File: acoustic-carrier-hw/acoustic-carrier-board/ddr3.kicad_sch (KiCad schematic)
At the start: 28 parts, among them IC1 ECP5-BGA256, IC2 MT41K256M16TW-107_P

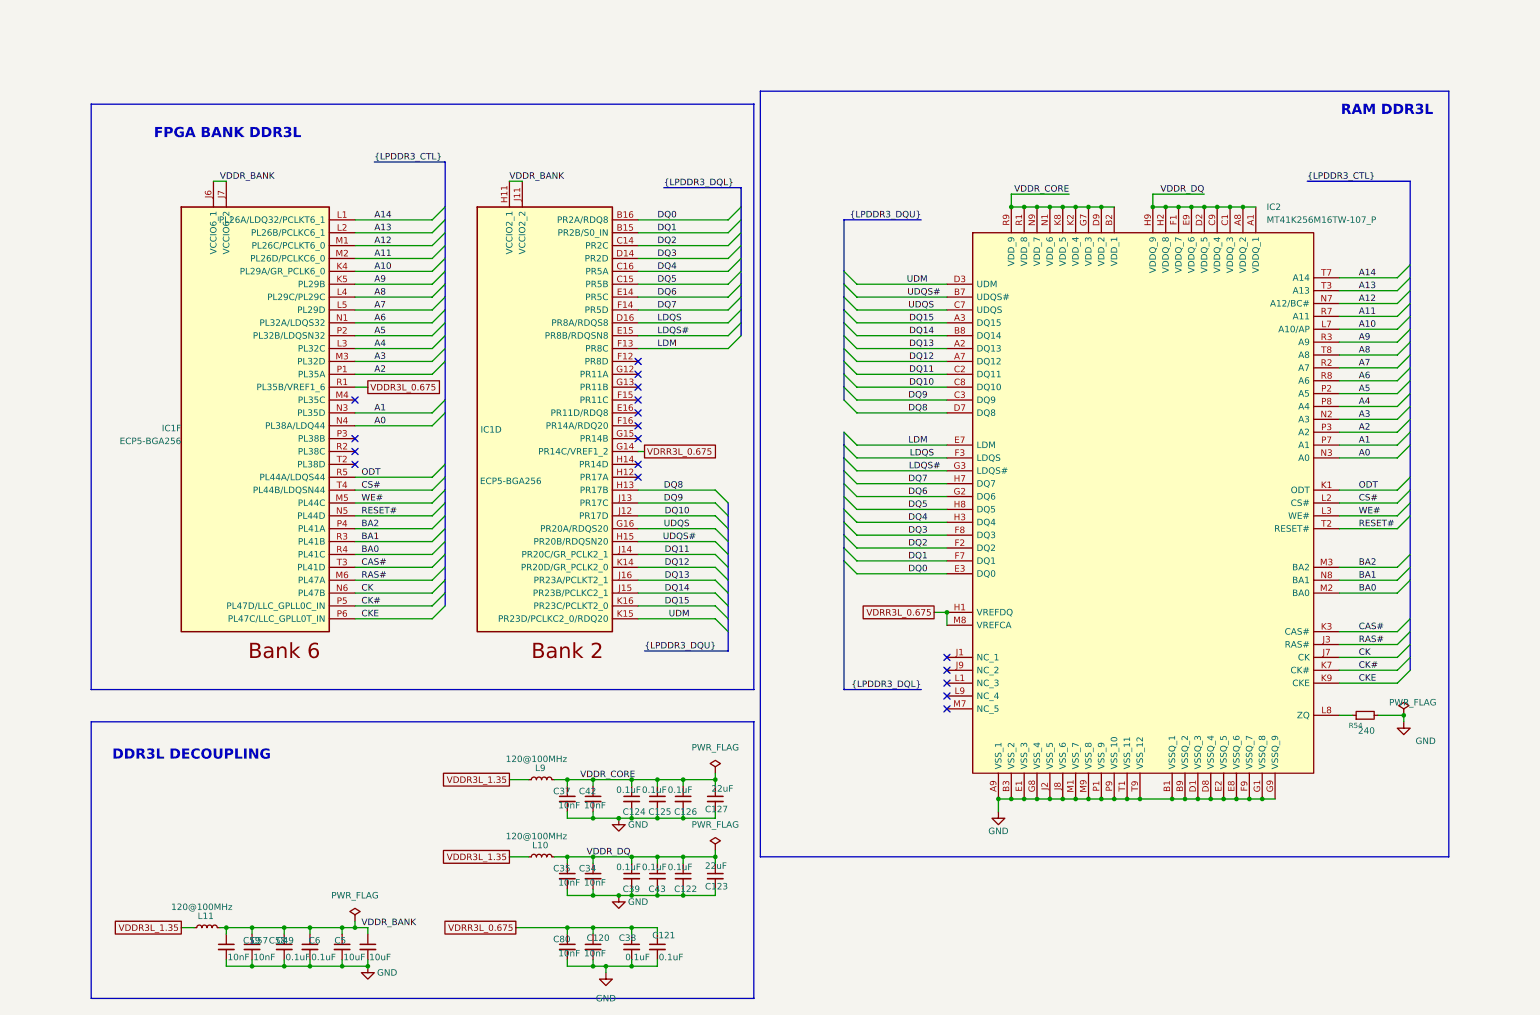
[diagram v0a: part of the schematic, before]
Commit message: [carrier] Added hierarchical labels
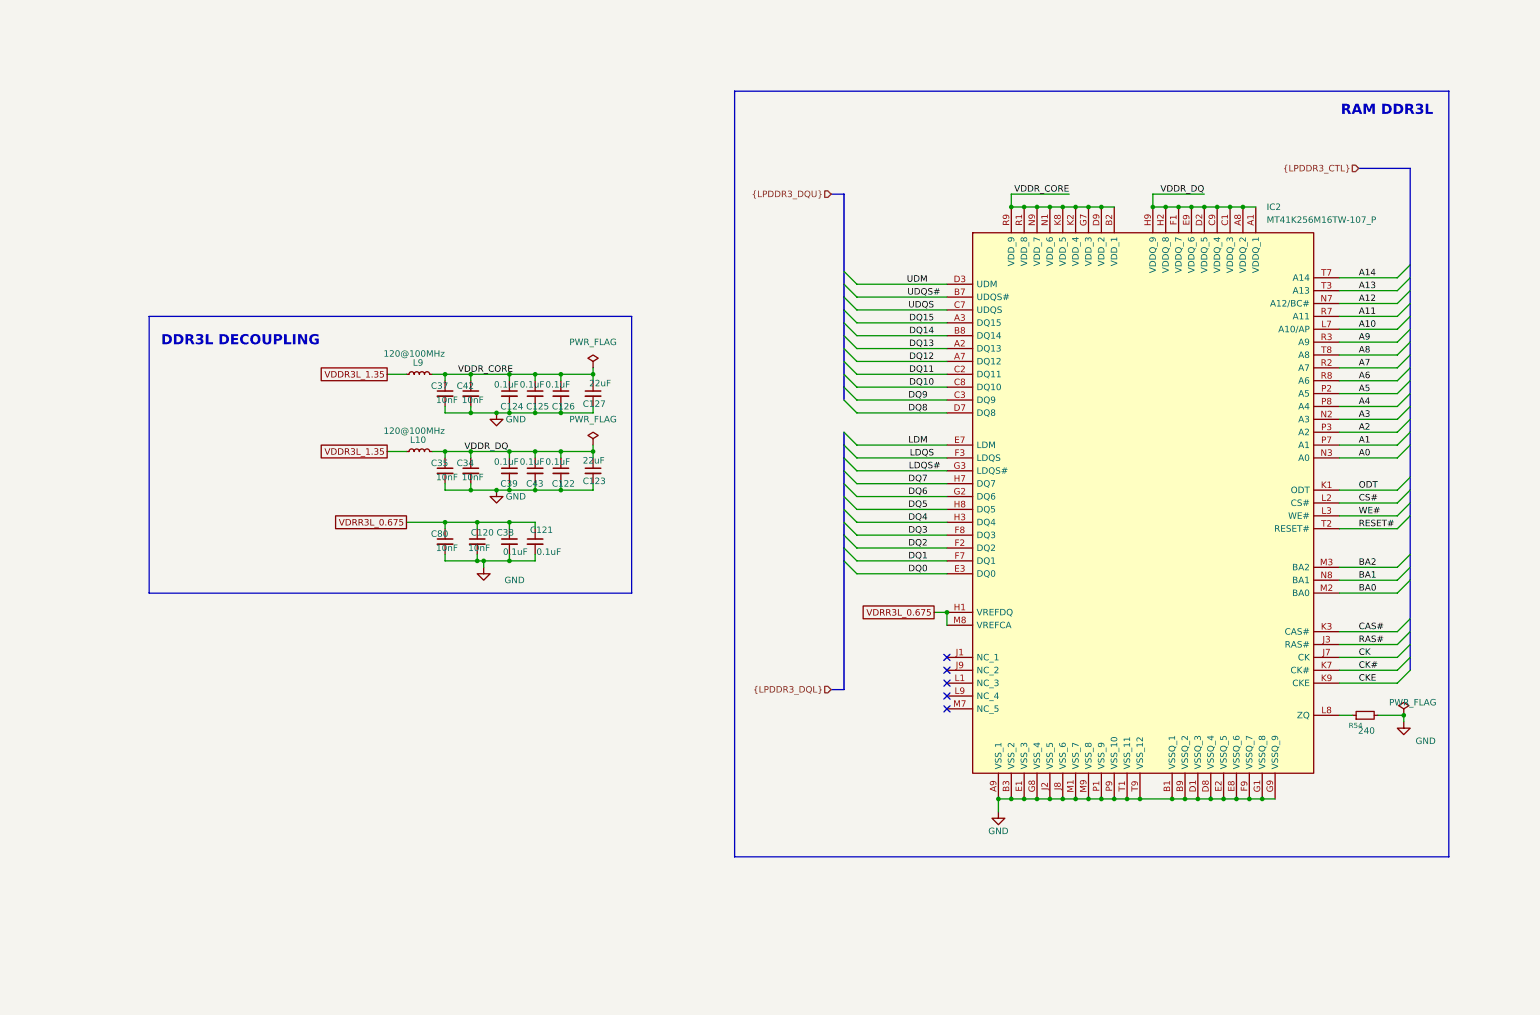
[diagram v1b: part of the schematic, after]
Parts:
- removed C49, C57: 0.1uF, Capacitor_SMD:C_0402_1005Metric, symbol Device:C_Small
- removed C5, C6: 10uF, Capacitor_SMD:C_0603_1608Metric, symbol Device:C_Small
- removed C58, C59: 10nF, Capacitor_SMD:C_0402_1005Metric, symbol Device:C_Small
- removed IC1: ECP5-BGA256, iw-fpga_mcu:BGA256C80P16X16_1400X1400X170, symbol iw-fpga_mcu:ECP5-BGA256
- removed L11: 120@100MHz, Inductor_SMD:L_0603_1608Metric, symbol Device:L_Small
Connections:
- no-connect marks 18 -> 5
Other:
- note removed: "FPGA BANK DDR3L"
- moved on the sheet: C120, C121, C122, C123, C124, C125, C126, C127, C34, C35, C37, C38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

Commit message: [carrier] Added decoupling caps to flash and comparators
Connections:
- net VDDR3L_1.35 renamed VLPDDR3_1.35
- net VDRR3L_0.675 renamed VLPDRR3_0.675
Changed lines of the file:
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@@
-	(wire
-		(pts
-			(xy 85.09 97.79) (xy 77.47 97.79)
-		)
-		(stroke
-			(width 0)
-			(type default)
-		)
-	)
 	(wire
 		(pts
@@
 	(wire
 		(pts
-			(xy 73.66 68.58) (xy 77.47 68.58)
+			(xy 72.39 68.58) (xy 77.47 68.58)
 		)
 		(stroke
@@
 		(pts
 			(xy 97.79 76.2) (xy 102.87 76.2)
+		)
+		(stroke
+			(width 0)
+			(type default)
+		)
+	)
+	(wire
+		(pts
+			(xy 73.66 97.79) (xy 85.09 97.79)
 		)
 		(stroke
@@
 		)
 	)
-	(global_label "VDDR3L_1.35"
+	(global_label "VLPDRR3_0.675"
 		(shape passive)
-		(at 73.66 68.58 180)
+		(at 73.66 97.79 180)
 		(fields_autoplaced yes)
 		(effects
@@
 		)
 		(property "Intersheetrefs" "${INTERSHEET_REFS}"
-			(at 59.449 68.58 0)
+			(at 56.9695 97.79 0)
 			(effects
 				(font
@@
 		)
 	)
-	(global_label "VDRR3L_0.675"
+	(global_label "VLPDDR3_1.35"
 		(shape passive)
-		(at 181.61 115.57 180)
+		(at 72.39 68.58 180)
 		(fields_autoplaced yes)
 		(effects
@@
 		)
 		(property "Intersheetrefs" "${INTERSHEET_REFS}"
-			(at 166.1895 115.57 0)
+			(at 56.909 68.58 0)
 			(effects
 				(font
@@
 		)
 	)
-	(global_label "VDRR3L_0.675"
+	(global_label "VLPDRR3_0.675"
 		(shape passive)
-		(at 77.47 97.79 180)
+		(at 181.61 115.57 180)
 		(fields_autoplaced yes)
 		(effects
@@
 		)
 		(property "Intersheetrefs" "${INTERSHEET_REFS}"
-			(at 62.0495 97.79 0)
+			(at 164.9195 115.57 0)
 			(effects
 				(font
@@
 		)
 	)
-	(global_label "VDDR3L_1.35"
+	(global_label "VLPDDR3_1.35"
 		(shape passive)
 		(at 73.66 83.82 180)
@@
 		)
 		(property "Intersheetrefs" "${INTERSHEET_REFS}"
-			(at 59.449 83.82 0)
+			(at 58.179 83.82 0)
 			(effects
 				(font

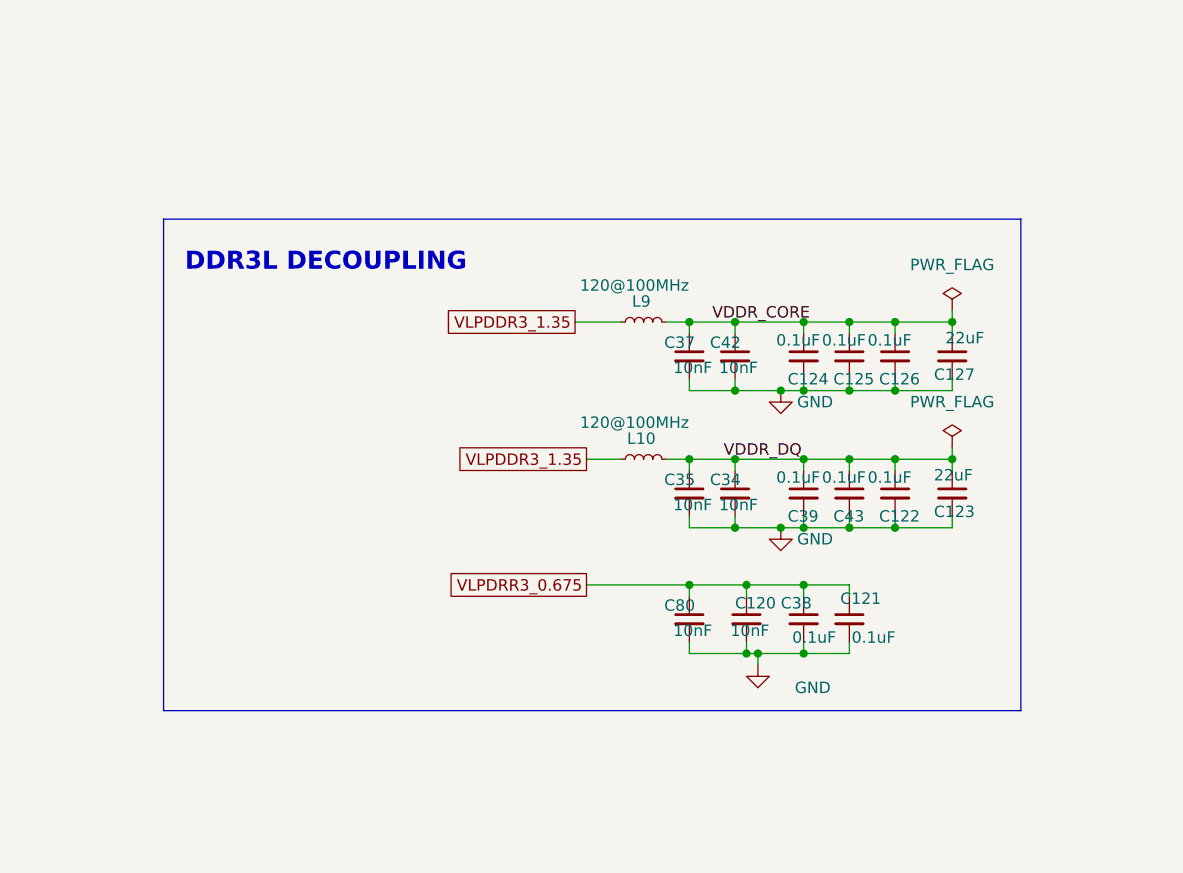
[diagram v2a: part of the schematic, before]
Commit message: [¢arrier] Did major cchecks of ETH, DDR, ANALOG, config (next) check buffer circuit driven by USB-CC, then start layout
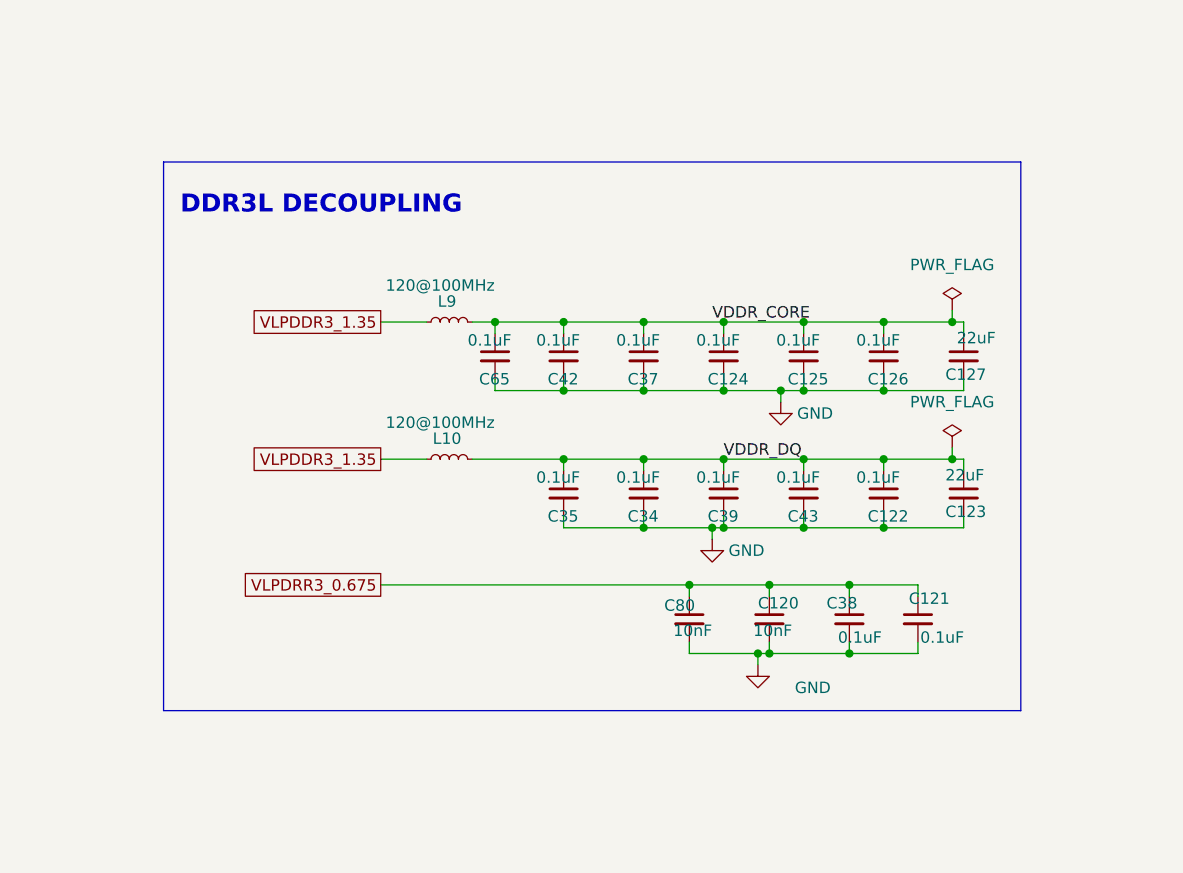
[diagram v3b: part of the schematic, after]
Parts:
- added C65: 0.1uF, Capacitor_SMD:C_0402_1005Metric, symbol Device:C_Small
- C34, C35, C37, C42: value 10nF -> 0.1uF; LPN CL05B103KB5NNNC -> C307331; MPN C15195 -> CL05B104KB54PNC
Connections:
- net GND: now also C65.2
- net VDDR_CORE: now also C65.1
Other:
- moved on the sheet: C120, C121, C122, C123, C124, C125, C126, C127, C38, C39, C43, L10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

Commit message: [carrier] Added testpoints
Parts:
- C120, C80: LPN CL05B103KB5NNNC -> C15195; MPN C15195 -> CL05B103KB5NNNC
- R54: LPN 0603WAF2400T5E -> C23350; MPN C23350 -> 0603WAF2400T5E
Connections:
- net A0 renamed DDR3.A0
- net A1 renamed DDR3.A1
- net A10 renamed DDR3.A10
- net A11 renamed DDR3.A11
- net A12 renamed DDR3.A12
- net A13 renamed DDR3.A13
- net A14 renamed DDR3.A14
- net A2 renamed DDR3.A2
- net A3 renamed DDR3.A3
- net A4 renamed DDR3.A4
- net A5 renamed DDR3.A5
- net A6 renamed DDR3.A6
- net A7 renamed DDR3.A7
- net A8 renamed DDR3.A8
- net A9 renamed DDR3.A9
- net BA0 renamed DDR3.BA0
- net BA1 renamed DDR3.BA1
- net BA2 renamed DDR3.BA2
- net CAS# renamed DDR3.CAS#
- net CK renamed DDR3.CK
- net CK# renamed DDR3.CK#
- net CKE renamed DDR3.CKE
- net CS# renamed DDR3.CS#
- net DQ0 renamed DDR3.DQ0
- net DQ1 renamed DDR3.DQ1
- net DQ10 renamed DDR3.DQ10
- net DQ11 renamed DDR3.DQ11
- net DQ12 renamed DDR3.DQ12
- net DQ13 renamed DDR3.DQ13
- net DQ14 renamed DDR3.DQ14
- net DQ15 renamed DDR3.DQ15
- net DQ2 renamed DDR3.DQ2
- net DQ3 renamed DDR3.DQ3
- net DQ4 renamed DDR3.DQ4
- net DQ5 renamed DDR3.DQ5
- net DQ6 renamed DDR3.DQ6
- net DQ7 renamed DDR3.DQ7
- net DQ8 renamed DDR3.DQ8
- net DQ9 renamed DDR3.DQ9
- net LDM renamed DDR3.LDM
- net LDQS renamed DDR3.LDQS
- net LDQS# renamed DDR3.LDQS#
- net ODT renamed DDR3.ODT
- net RAS# renamed DDR3.RAS#
- net RESET# renamed DDR3.RESET#
- net UDM renamed DDR3.UDM
- net UDQS renamed DDR3.UDQS
- net UDQS# renamed DDR3.UDQS#
- net VLPDDR3_1.35 renamed VLPDDR3_1V35
- net VLPDRR3_0.675 renamed VLPDRR3_V675
- net WE# renamed DDR3.WE#
